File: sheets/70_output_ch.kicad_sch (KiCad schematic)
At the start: 12 parts, among them Q701 DMN10H220LQ, U701 74AHCT1G126

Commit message: [Claude Code] esquema+PCB: campos LCSC y sustitutos PROTO del BOM (pcb-v1-rc2)
- Esquema (solo campos, ocultos): LCSC en todos los componentes; MPN_PROTO,
  LCSC_PROTO y Manufacturer_PROTO con los sustitutos aceptados; Notes con
  compra y montaje (Q101, Q102, F101, L201, U503 a mano desde DigiKey/Mouser).
  MPN (PROD), valores, huellas y conexiones sin cambios. LCSC Part -> LCSC.
- PCB: mismos campos en las 145 huellas, insertados como texto (equivalente
  a F8 solo para campos); nada cambia fuera de las huellas.
- ERC por hoja igual que antes (0 errores, 5 avisos). DRC 0 errores / 3 avisos
  aceptados, 0 sin rutear, paridad 0 (antes de sincronizar: 145).
- etapa6_fab.py usa los campos _PROTO y genera bom_jlc_lcsc.csv; este y
  cpl_jlc.csv salen idénticos (60 líneas, 123 piezas). Gerbers sin cambios
  de contenido.

Co-Authored-By: Claude Opus 5.5 <noreply@anthropic.com>
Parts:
- C702: LCSC (none) -> C85864; LCSC_PROTO (none) -> C14663; MPN_PROTO (none) -> CC0603KRX7R9BB104; Manufacturer_PROTO (none) -> Yageo; Notes Desacople de U701. -> Desacople de U701. PROTO (2026-10-30): Yageo CC0603KRX7R9BB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
- D701: LCSC (none) -> C123816
- D703: LCSC (none) -> C85087
- D704: LCSC (none) -> C500776
- Q701: LCSC (none) -> C5260572; LCSC_PROTO (none) -> C102615
- R702: LCSC (none) -> C116697; LCSC_PROTO (none) -> C23162; MPN_PROTO (none) -> 0603WAF4701T5E; Manufacturer_PROTO (none) -> UNI-ROYAL; Notes Gate en serie: limita la corriente de carga del gate desde el buffer. -> Gate en serie: limita la corriente de carga del gate desde el buffer. PROTO (2026-10-30): UNI-ROYAL 0603WAF4701T5E (LCSC C23162, JLC basic), misma especificación, sin AEC-Q200.
- R703: LCSC (none) -> C116674; LCSC_PROTO (none) -> C25803; MPN_PROTO (none) -> 0603WAF1003T5E; Manufacturer_PROTO (none) -> UNI-ROYAL; Notes Pull-down de gate: Q701 apagado sin +5V_VEH. -> Pull-down de gate: Q701 apagado sin +5V_VEH. PROTO (2026-10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
- R708, R709: LCSC (none) -> C144522
- R710: LCSC (none) -> C144681
- R711: LCSC (none) -> C116674; LCSC_PROTO (none) -> C25803; MPN_PROTO (none) -> 0603WAF1003T5E; Manufacturer_PROTO (none) -> UNI-ROYAL; Notes Pull-down de EN: salida apagada mientras el MCU esta en reset o el GPIO flota. -> Pull-down de EN: salida apagada mientras el MCU esta en reset o el GPIO flota. PROTO (2026-10-30): UNI-ROYAL 0603WAF1003T5E (LCSC C25803, JLC basic), misma especificación, sin AEC-Q200.
- U701: LCSC_PROTO (none) -> C163712; Notes Traslada EN de 3.3 V (MCU) a 5 V para el gate (DMN10H220LQ especifica RDS a 4.5 V). Entrada TTL: VIH 2 V. OE a VCC. Sin +5V_VEH la salida queda baja. -> Traslada EN de 3.3 V (MCU) a 5 V para el gate (DMN10H220LQ especifica RDS a 4.5 V). Entrada TTL: VIH 2 V. OE a VCC. Sin +5V_VEH la salida queda baja. PROD (2026-10-30): sin stock suficiente en JLC/LCSC para 100 placas; comprar en DigiKey/Mouser.

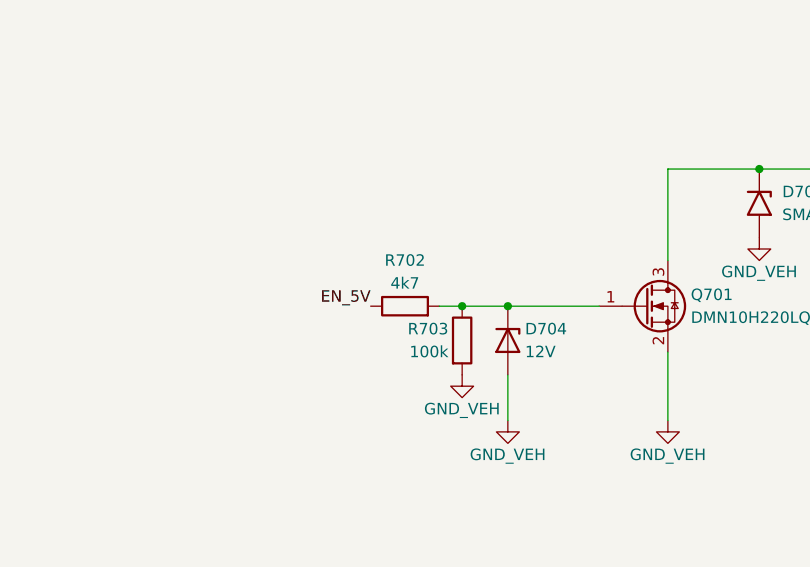
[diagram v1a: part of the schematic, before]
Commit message: [Claude Code] bom: compra principal en LCSC + DigiKey/Mouser; consolidación de pasivos
- Plan: JLC solo PCB + stencil Top; componentes de LCSC soldados a mano.
- Consolidación (solo valor/campos): R702/R752 4k7 → 2.2k; 23 × 100 nF a un
  MPN de 100 V X7R; PROTO 1 µF 50 V y 10 µF 25 V X7R. BOM PROTO 70 → 68 líneas.
- LCSC_BOM_COMPLETO_PROTO.csv: 6 juegos, 62 líneas, USD 552.43 (3 juegos: 286.65).
- DIGIKEY_MOUSER.csv: L201, U503, Q101, Q102, F101 (0 en LCSC), ≈ USD 99.54.
- Resumen de costos en BOM_SOURCING.md; archivos de JLC al día como alternativa.
- DRC 0 errores / 3 avisos aceptados, paridad 0, ERC 0 / 5.

Co-Authored-By: Claude Opus 5.5 <noreply@anthropic.com>
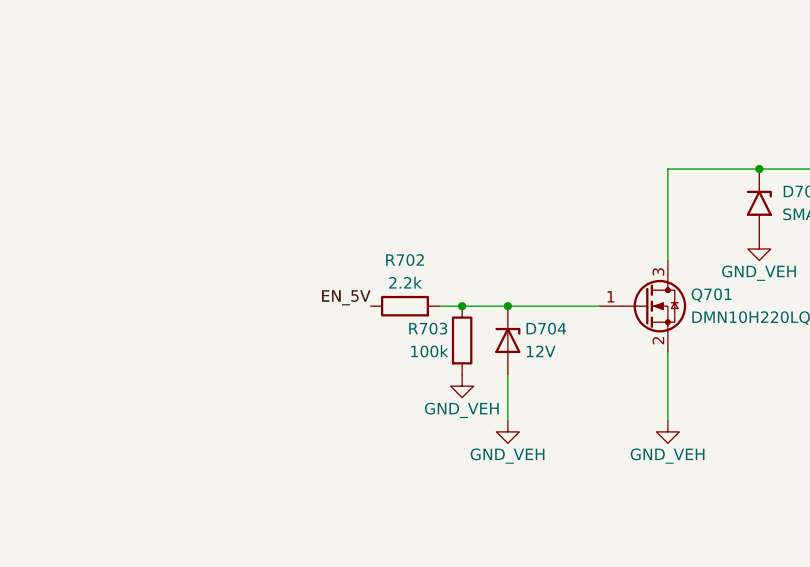
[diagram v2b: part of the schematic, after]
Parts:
- C702: LCSC C85864 -> C415406; LCSC_PROTO C14663 -> C88219; MPN GCM188R71H104KA57D -> GCM188R72A104KA64D; MPN_PROTO CC0603KRX7R9BB104 -> 0603B104K101NT; Manufacturer_PROTO Yageo -> FH; Notes Desacople de U701. PROTO (2026-10-30): Yageo CC0603KRX7R9BB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 -> Desacople de U701. PROTO (2026-10-30, consolidacion): un so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
- R702: value 4k7 -> 2.2k; LCSC C116697 -> C125931; LCSC_PROTO C23162 -> C4190; MPN AC0603FR-074K7L -> AC0603FR-072K2L; MPN_PROTO 0603WAF4701T5E -> 0603WAF2201T5E; Notes Gate en serie: limita la corriente de carga del gate desde 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 -> Gate en serie desde el 74AHCT1G126 (5 V): 2.2k, el mismo va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
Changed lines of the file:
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@@
 			)
 		)
-		(property "MPN" "GCM188R71H104KA57D"
+		(property "MPN" "GCM188R72A104KA64D"
 			(at 99.06 143.51 0)
 			(hide yes)
@@
 			)
 		)
-		(property "Notes" "Desacople de U701. PROTO (2026-10-30): Yageo CC0603KRX7R9BB104 (LCSC C14663, JLC basic), misma especificación, sin AEC-Q200."
+		(property "Notes" "Desacople de U701. PROTO (2026-10-30, consolidacion): un solo MPN para los 100 nF 0603: 100 V X7R (FH 0603B104K101NT, LCSC C88219), sin AEC-Q200. PROD: Murata GCM188R72A104KA64D (100 V, AEC-Q200). Mismo valor y tolerancia."
 			(at 99.06 143.51 0)
 			(hide yes)
@@
 			)
 		)
-		(property "LCSC" "C85864"
+		(property "LCSC" "C415406"
 			(at 99.06 143.51 0)
 			(hide yes)
@@
 			)
 		)
-		(property "MPN_PROTO" "CC0603KRX7R9BB104"
+		(property "MPN_PROTO" "0603B104K101NT"
 			(at 99.06 143.51 0)
 			(hide yes)
@@
 			)
 		)
-		(property "Manufacturer_PROTO" "Yageo"
+		(property "Manufacturer_PROTO" "FH"
 			(at 99.06 143.51 0)
 			(hide yes)
@@
 			)
 		)
-		(property "LCSC_PROTO" "C14663"
+		(property "LCSC_PROTO" "C88219"
 			(at 99.06 143.51 0)
 			(hide yes)
@@
 			)
 		)
-		(property "Value" "4k7"
+		(property "Value" "2.2k"
 			(at 194.31 107.95 90)
 			(show_name no)
@@
 			)
 		)
-		(property "MPN" "AC0603FR-074K7L"
+		(property "MPN" "AC0603FR-072K2L"
 			(at 194.31 110.49 0)
 			(hide yes)
@@
 			)
 		)
-		(property "Notes" "Gate en serie: limita la corriente de carga del gate desde el buffer. PROTO (2026-10-30): UNI-ROYAL 0603WAF4701T5E (LCSC C23162, JLC basic), misma especificación, sin AEC-Q200."
+		(property "Notes" "Gate en serie desde el 74AHCT1G126 (5 V): 2.2k, el mismo valor que R803/R804 (una linea de BOM). Con el pull-down de 100k, Vgs = 4.89 V (antes 4.78 V con 4k7); pico de carga 2.3 mA (el buffer da 8 mA). PROTO (2026-10-30, consolidacion): UNI-ROYAL 0603WAF2201T5E (LCSC C4190), sin AEC-Q200."
 			(at 194.31 110.49 0)
 			(hide yes)
@@
 			)
 		)
-		(property "LCSC" "C116697"
+		(property "LCSC" "C125931"
 			(at 194.31 110.49 0)
 			(hide yes)
@@
 			)
 		)
-		(property "MPN_PROTO" "0603WAF4701T5E"
+		(property "MPN_PROTO" "0603WAF2201T5E"
 			(at 194.31 110.49 0)
 			(hide yes)
@@
 			)
 		)
-		(property "LCSC_PROTO" "C23162"
+		(property "LCSC_PROTO" "C4190"
 			(at 194.31 110.49 0)
 			(hide yes)
